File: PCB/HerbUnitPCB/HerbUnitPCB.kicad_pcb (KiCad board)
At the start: 2 copper layers, 57.4 x 61.5 mm, 48 parts, among them J1 USB_C_Receptacle_USB2.0_16P, J2 Barrel_Jack_Switch_Pin3Ring, J3 Conn_01x03_Pin, J4 SD_Card_Device, J5 Screw_Terminal_01x02, J6 Conn_01x03_Pin, SW1 SW_Push, SW2 SW_Push, SW3 SW_Push, U1 USBLC6-2P6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

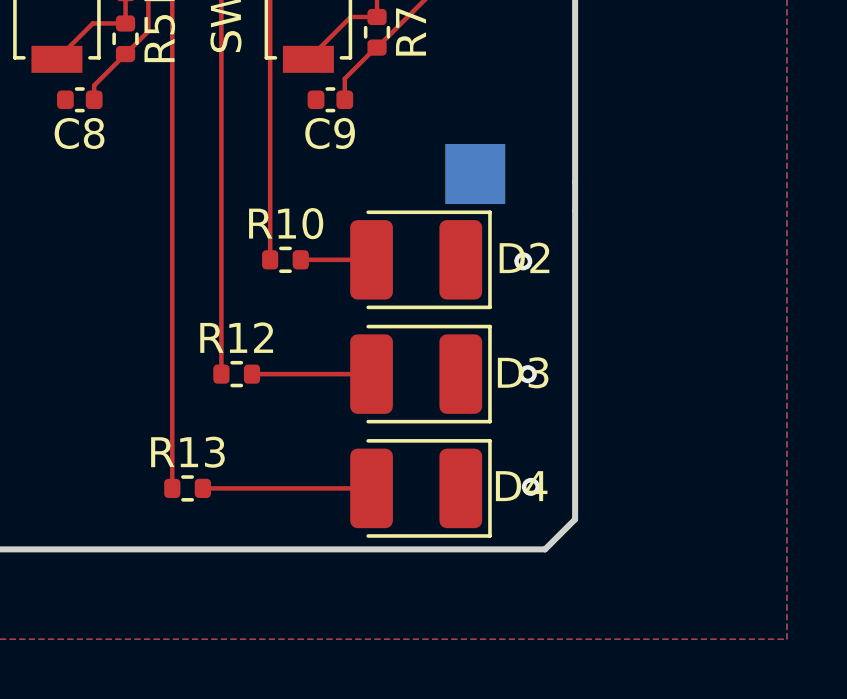
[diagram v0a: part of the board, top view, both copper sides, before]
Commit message: Changed LED footprints
Thnx Robert :)
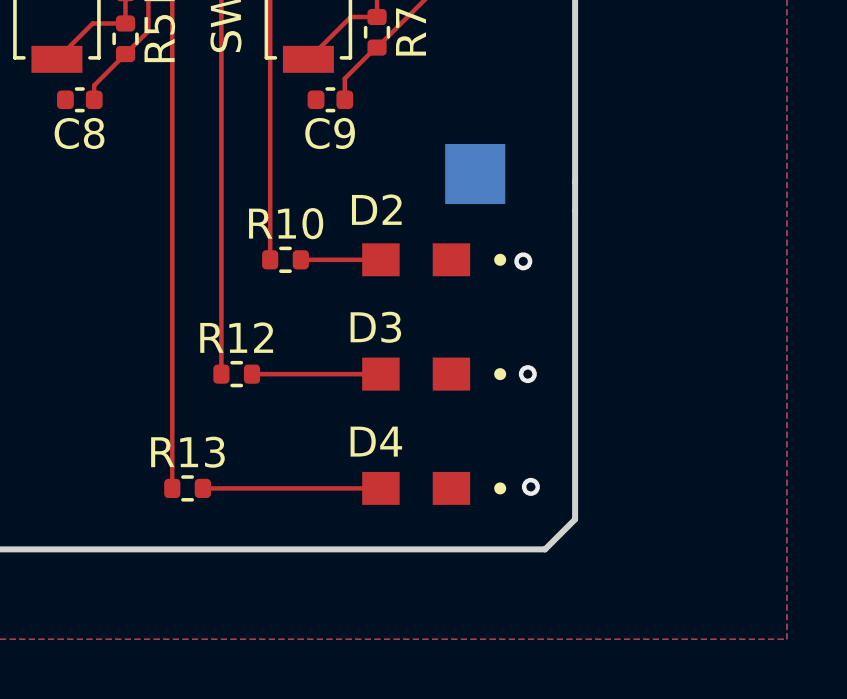
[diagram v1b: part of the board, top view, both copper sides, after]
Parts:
- D2: value LED -> Green; footprint LED_SMD:LED_1210_3225Metric_Pad1.42x2.65mm_HandSolder -> GreenLED:LED_APT2012CGCK
- D3: value LED -> Blue; footprint LED_SMD:LED_1210_3225Metric_Pad1.42x2.65mm_HandSolder -> BlueLED:LED_APT2012VBC_D
- D4: value LED -> Red; footprint LED_SMD:LED_1210_3225Metric_Pad1.42x2.65mm_HandSolder -> RedLED:LED_APT2012EC
- D5, D6: value Green LED -> Green
